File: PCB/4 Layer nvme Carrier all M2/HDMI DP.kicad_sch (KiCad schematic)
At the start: 58 parts, among them J4 HDMI_A, Q1 2N7002, Q2 2SK3018, Q3 2SK3018, Q4 2SK3018, Q79 2N7002, U1 TPAZ1023-04F, U2 TPAZ1023-04F, U81 TPAZ1023-04F, U82 TPAZ1023-04F

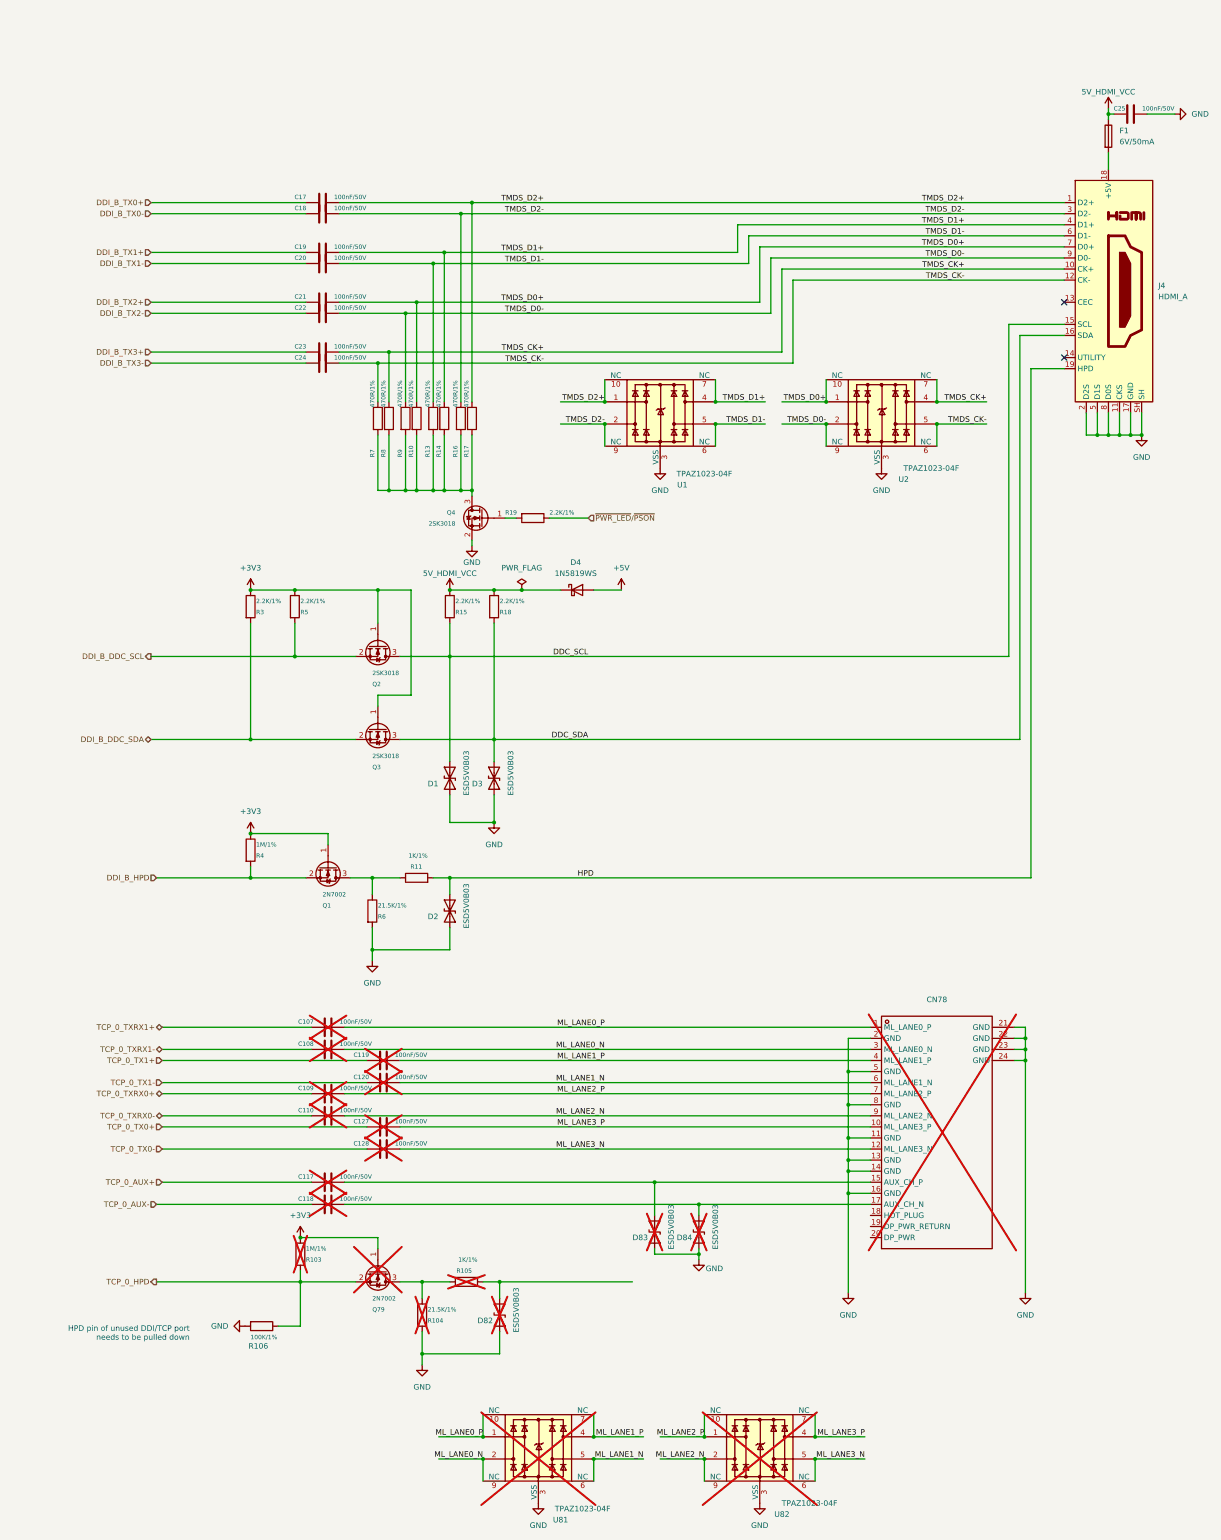
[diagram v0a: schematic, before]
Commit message: first all-M.2 version
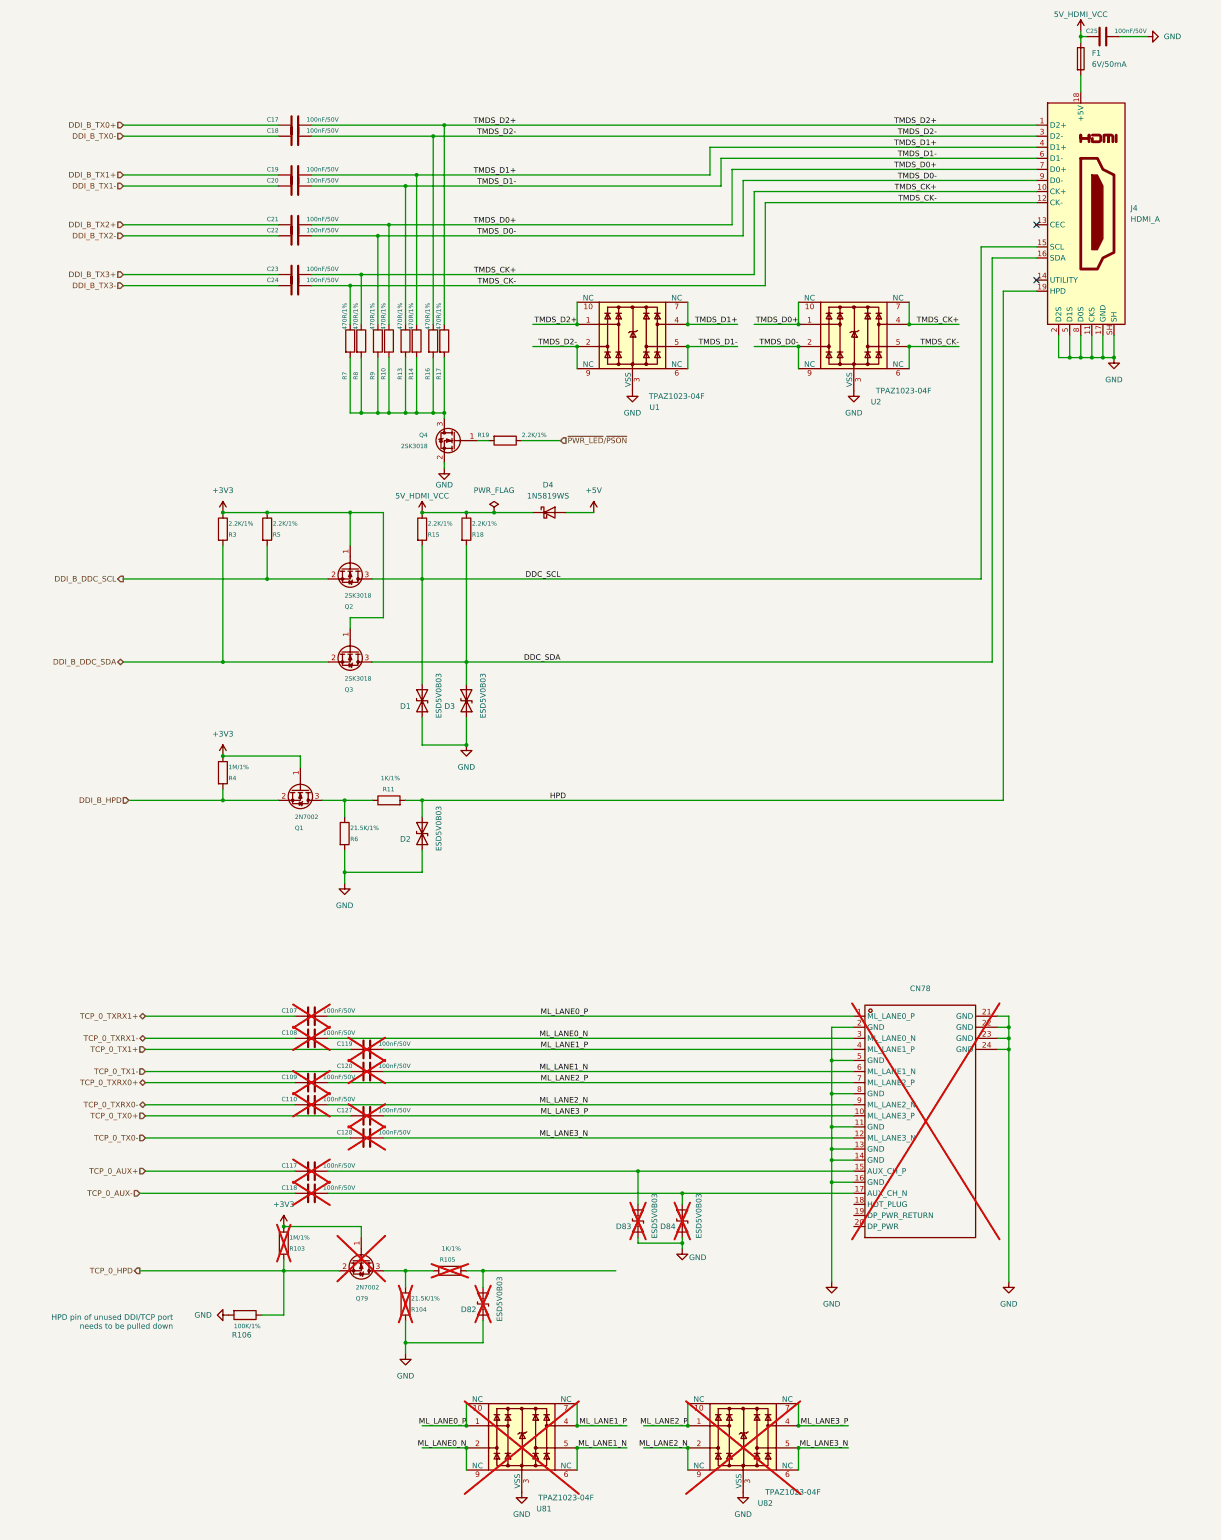
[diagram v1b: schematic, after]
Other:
- moved on the sheet: C107, C108, C109, C110, C117, C118, C119, C120, C127, C128, C17, C18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
